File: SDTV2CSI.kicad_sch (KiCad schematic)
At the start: 70 parts, among them J1 Conn_Coaxial, J2 Conn_Coaxial, J3 SFW15R-1STE1LF, J4 5-2301994-9, U1 ADV7280AWBCPZ-M, U2 TLV75718PDBV, U3 XR22800IL32TR-F, U4 MP8007GV-Z, Y1 28.63636MHz

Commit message: update and considering losing poe for waveshare OTS
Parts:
- removed J4: 5-2301994-9, Connector_RJ:RJ45_Bel_SI-60062-F, symbol Connector:RJ45_Bel_SI-60062-F
- added C28, C29: 0.01μF, Capacitor_SMD:C_0402_1005Metric, symbol Device:C_Small
- added D4: BR, Diode_SMD:Diode_Bridge_Diotec_SO-DIL-Slim, symbol Diode_Bridge:DF01S1
- added D5: SBR8U60P5-13, symbol Device:D_Small
- added FB1, FB2: 30m, Inductor_SMD:L_0603_1608Metric, symbol Device:FerriteBead_Small
- added L1: L_Small, symbol Device:L_Small
- added P1: Pi Zero, AU:PIZERO, symbol AU:Pi Zero
- added P2: TMJ19911ADNL, AU:7498210220A, symbol AU:TMJ19911ADNL
- added TR1: CX9628, AU:SMT_29-ALD_COC, symbol AU:CX9628
- J3: footprint AU:528061510 -> AU:CON15_1X15_DRB_SFW_GLE
- R19: value 8.06k -> 7.5k; Alt PN (none) -> CR0402-FX-7501GLF; MPN RC0402FR-078K06L -> WR04X7501FTL; Manufacturer YAGEO -> Walsin Technology Corporation
- R22: value 41.2 -> 576; MPN RC0402FR-0741R2L -> RC0402FR-07576RL
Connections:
- net ER+: now also P2.4 (RD+)
- net ER-: now also P2.6 (RD-)
- net ET+: now also P2.1 (TD+)
- net ET-: now also P2.3 (TD-)
- net at U4.1 (AUX): now also R18.2, R19.1
- net sw: now reaches U4.12 (SW)
- net sw: now also U4.13 (SW__1), TR1.3
- net GNDD: now reaches U4.16 (GND)
- net GNDD: now also U4.17 (GND__1), U4.29 (GND__2), TR1.5
- net VSS: now reaches U4.23 (VSS)
- net VSS: now also U4.24 (VSS__1)
- net at U4.26 (CLASS): now also R22.2
- net VDD: now reaches U4.4 (VDD)
- net VDD: now also R8.1, C29.1, FB1.2, L1.2
- net Vss: now reaches R22.1
- net Vss: now also C29.2, FB2.1
- net SCL renamed CSCL
- net SDA renamed CSDA
- new net: D5.2 (A), TR1.10, TR1.9
- new net: L1.1, TR1.1
- new net CT1: D4.4, P2.2 (CT)
- new net CT2: D4.3, P2.5 (CT)
- new net GNDA: TR1.6, TR1.7
- new net PoEGND: C28.1, D4.2 (-), FB2.2
- new net PoEVDD: C28.2, D4.1 (+), FB1.1
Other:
- moved on the sheet: C1, C10, C11, C12, C13, C14, C15, C16, C17, C18, C19, C2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

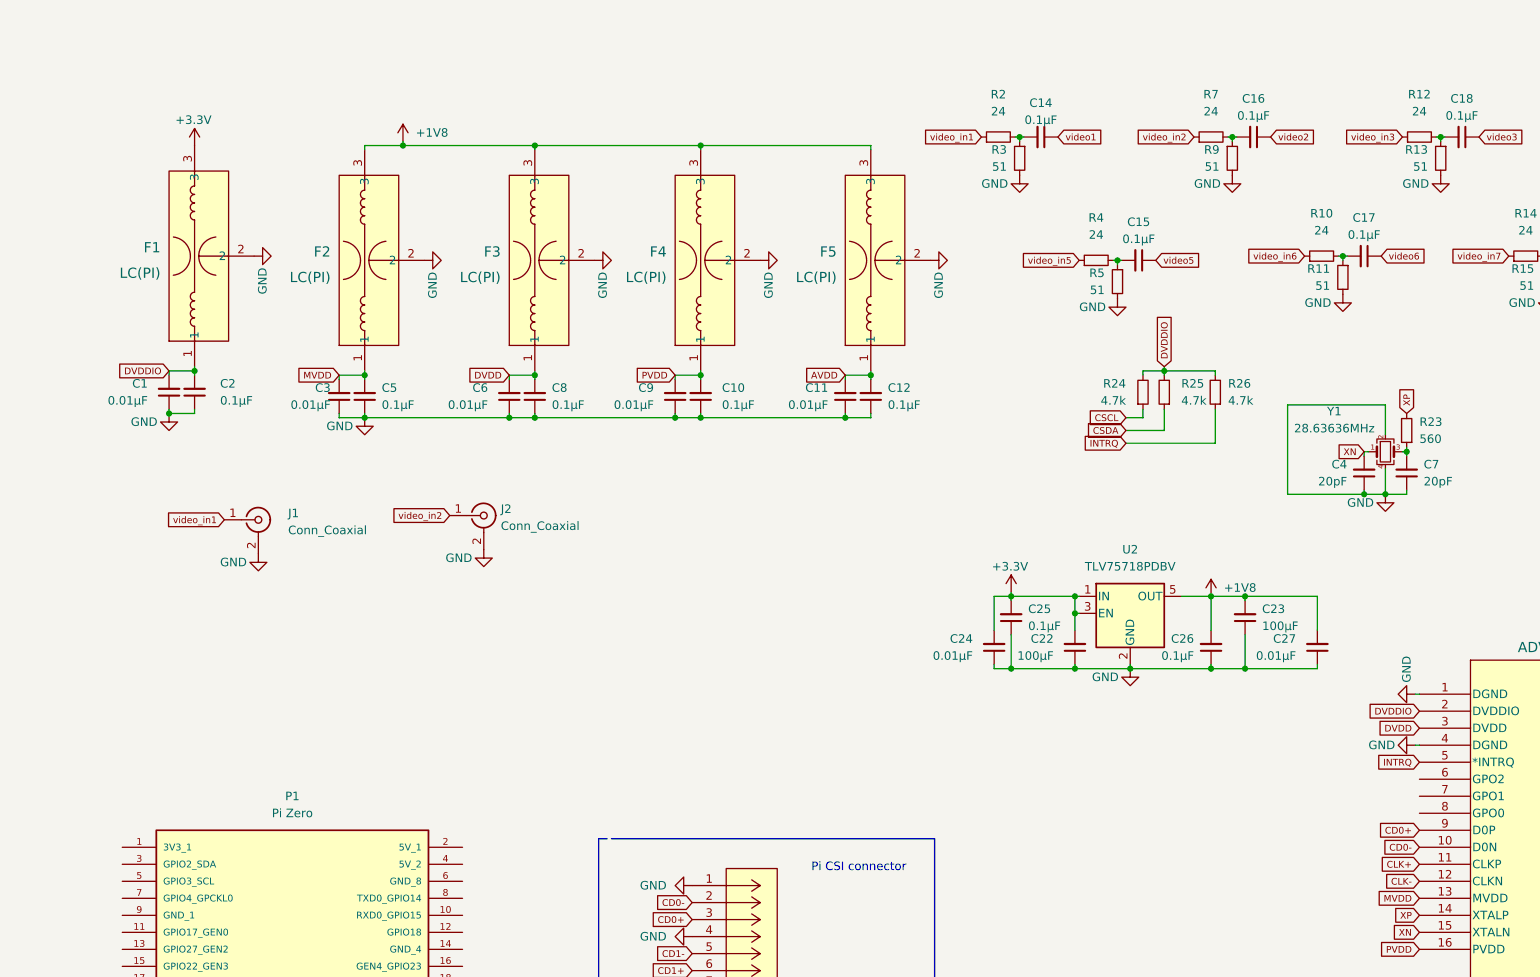
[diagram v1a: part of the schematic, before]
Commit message: working on converting back to 0201
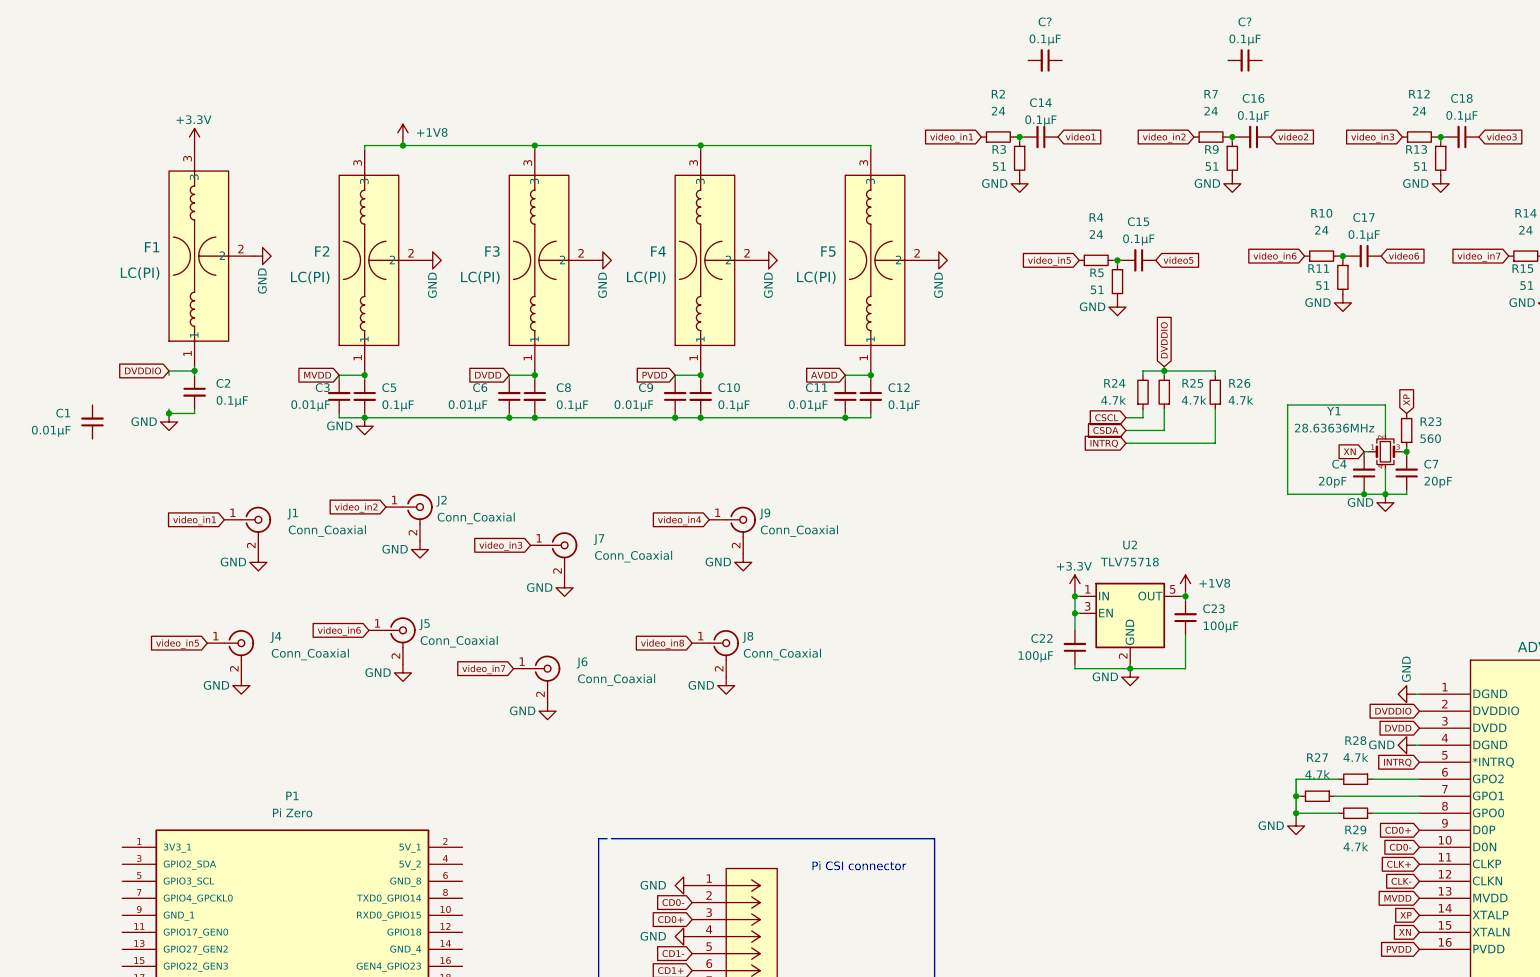
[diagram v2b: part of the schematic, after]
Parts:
- removed C24, C27: 0.01μF, Capacitor_SMD:C_0402_1005Metric, symbol Device:C_Small
- removed C25, C26: 0.1μF, Capacitor_SMD:C_0402_1005Metric, symbol Device:C_Small
- added C? (x2): 0.1μF, AU:R_0201_0603Metric, symbol Device:C_Small
- added J4, J5, J6, J7, J8, J9: Conn_Coaxial, Connector_Coaxial:SMA_Amphenol_901-144_Vertical, symbol Connector:Conn_Coaxial
- added R27, R28, R29: 4.7k, Resistor_SMD:R_0402_1005Metric, symbol Device:R_Small
- C10, C12, C2, C5, C8: footprint Capacitor_SMD:C_0402_1005Metric -> AU:R_0201_0603Metric; JLCPCB PN C60474 -> (none); MPN CC0402KRX7R7BB104 -> GRM033Z71C104KE14D; Manufacturer YAGEO -> Murata Electronics
- U2: value TLV75718PDBV -> TLV75718
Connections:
- net AVDD: now also C12.1; no longer C12.2
- net DVDD: now also C8.1; no longer C8.2
- net DVDDIO: now also C2.1; no longer C1.2, C2.2
- net GND: now also C10.2, C12.2, C2.2, C5.2, C8.2, J4.2 (Ext), J5.2 (Ext), J6.2 (Ext), J7.2 (Ext), J8.2 (Ext), J9.2 (Ext), R27.2, R28.2, R29.2; no longer C1.1, C10.1, C12.1, C2.1, C5.1, C8.1
- net MVDD: now also C5.1; no longer C5.2
- net PVDD: now also C10.1; no longer C10.2
- net video_in3: now also J7.1 (In)
- net video_in4: now also J9.1 (In)
- net video_in5: now also J4.1 (In)
- net video_in6: now also J5.1 (In)
- net video_in7: now also J6.1 (In)
- net video_in8: now also J8.1 (In)
- net at U1.6 (GPO2): now also R28.1
- net at U1.7 (GPO1): now also R27.1
- net at U1.8 (GPO0): now also R29.1
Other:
- moved on the sheet: C1, C23, J2

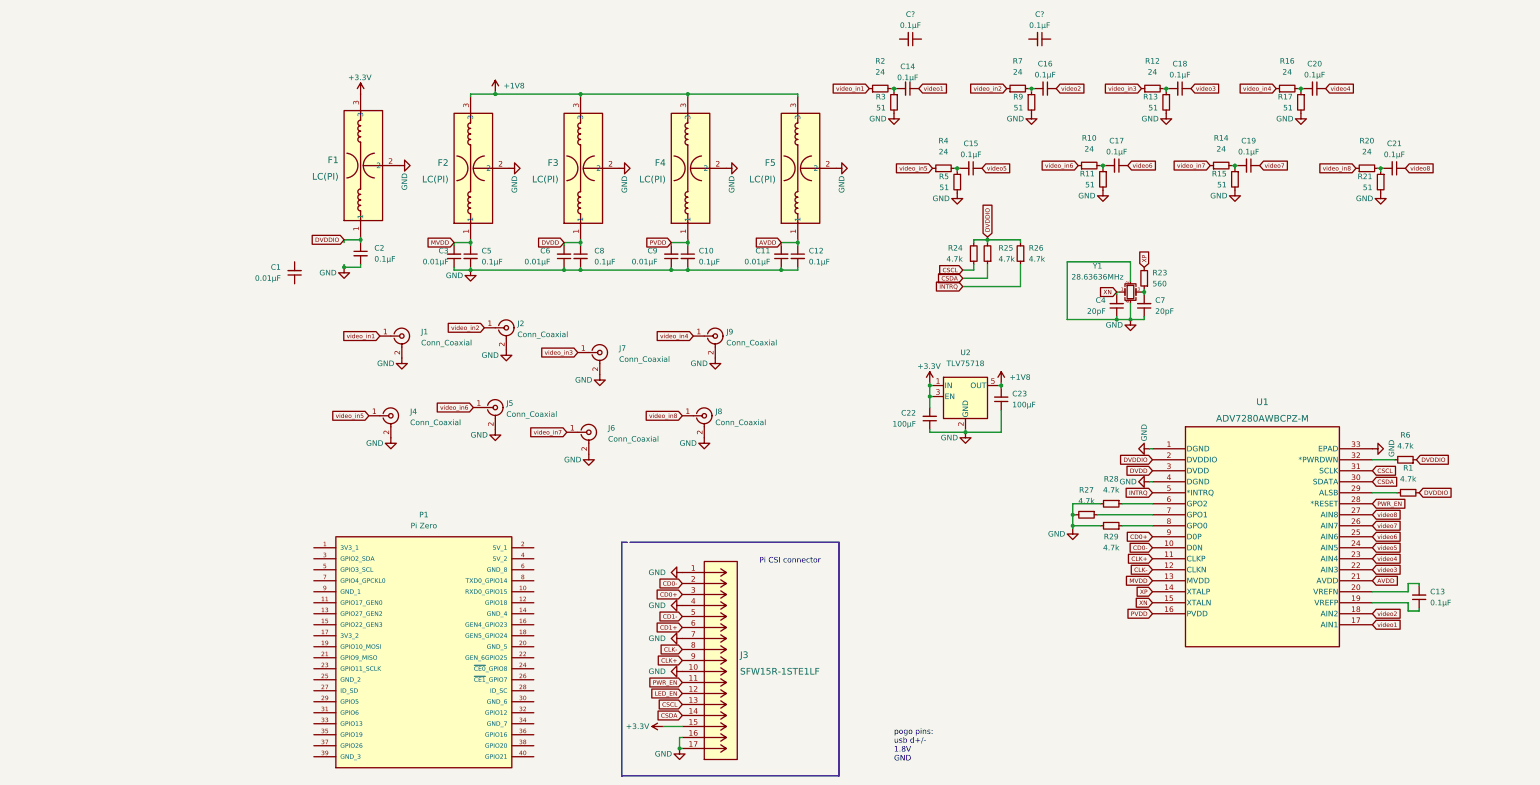
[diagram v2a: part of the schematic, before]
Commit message: will remove PoE components commit for posterity
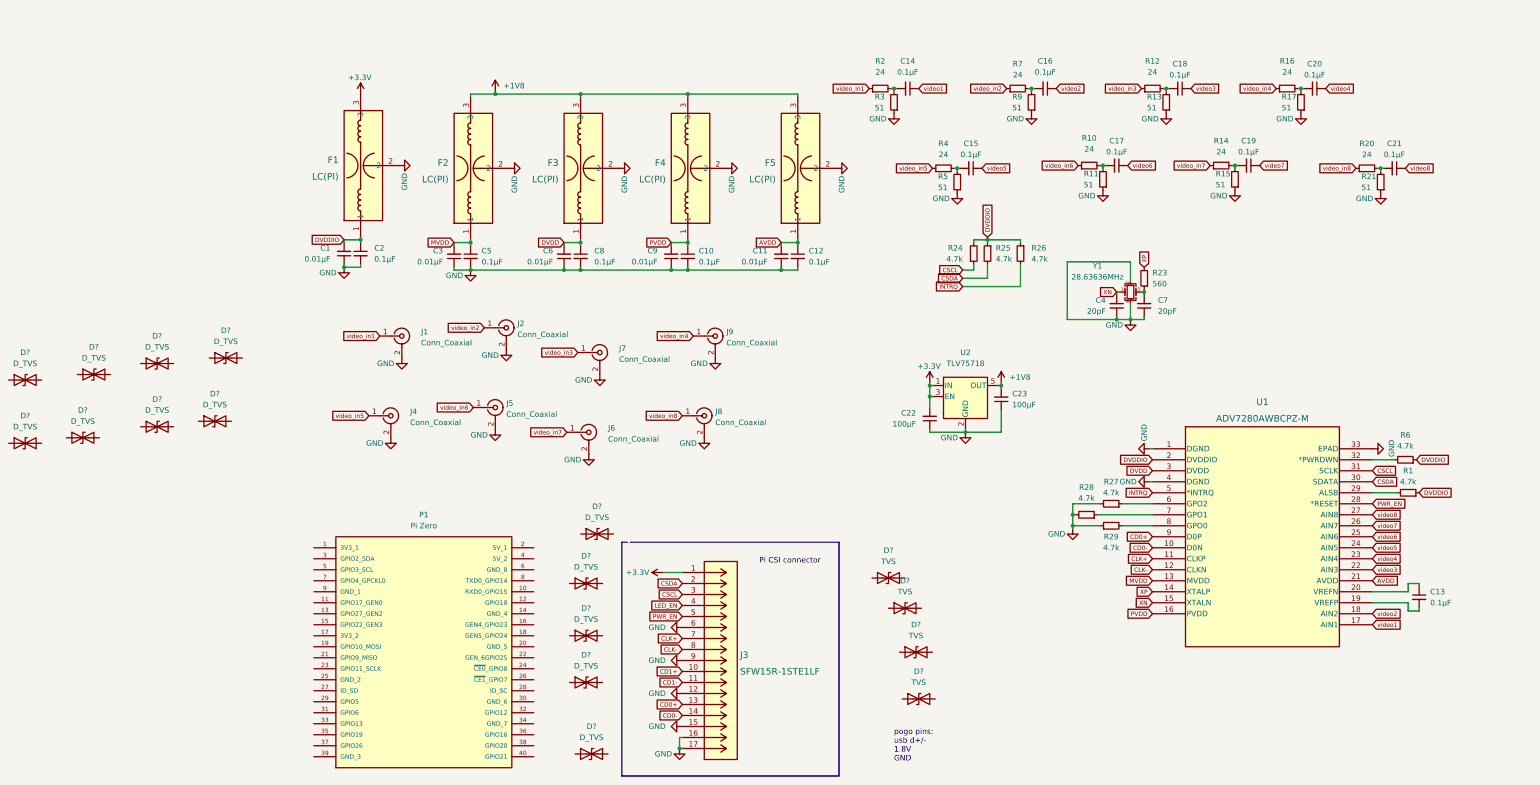
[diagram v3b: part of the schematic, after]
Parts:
- removed C14, C16: 0.1μF, Capacitor_SMD:C_0402_1005Metric, symbol Device:C_Small
- added D? (x13): D_TVS, AU:R_0201_0603Metric, symbol Device:D_TVS
- added D? (x4): TVS, AU:R_0201_0603Metric, symbol Device:D_TVS
- C1, C11, C3, C6, C9: footprint Capacitor_SMD:C_0402_1005Metric -> AU:R_0201_0603Metric; JLCPCB PN C15195 -> (none); MPN CL05B103KB5NNNC -> GRM033R71E103KE14D; Manufacturer Samsung Electro-Mechanics -> Murata Electronics; Voltage 50V -> 25V
- C13: footprint Capacitor_SMD:C_0402_1005Metric -> AU:R_0201_0603Metric; JLCPCB PN C60474 -> (none); MPN CC0402KRX7R7BB104 -> GRM033Z71C104KE14D; Manufacturer YAGEO -> Murata Electronics
- C4, C7: footprint Capacitor_SMD:C_0402_1005Metric -> AU:R_0201_0603Metric; JLCPCB PN C437436 -> (none); MPN GRT1555C1H200FA02D -> GRM0335C1H200GA01D; Tolerance 1% -> (none)
- R1, R24, R25, R26, R27, R28, R29, R6: footprint Resistor_SMD:R_0402_1005Metric -> Resistor_SMD:R_0201_0603Metric; JLCPCB PN C105870 -> (none); MPN RC0402JR-074K7L -> CR0201-JW-472GLF; Manufacturer YAGEO -> Bourns Inc.; Power 1/16W -> 1/20W; Stock on hand (none) -> 10k
- R2, R7: footprint Resistor_SMD:R_0402_1005Metric -> Resistor_SMD:R_0201_0603Metric; JLCPCB PN C274890 -> (none); MPN RT0402FRE0724RL -> ERJ-1GNF24R0C; Manufacturer YAGEO -> Panasonic Electronic Components; Power 1/16W -> 1/20W
- R23: footprint Resistor_SMD:R_0402_1005Metric -> AU:R_0201_0603Metric; Alt PN (none) -> CRCW0201560RFKED; JLCPCB PN C163460 -> (none); MPN CR0402-FX-5600GLF -> ERA-1AEB561C; Manufacturer Bourns Inc. -> Panasonic Electronic Components; Tolerance (none) -> 1%
- R3, R9: footprint Resistor_SMD:R_0402_1005Metric -> Resistor_SMD:R_0201_0603Metric; JLCPCB PN C227127 -> (none); MPN RT0402FRE0751RL -> RMCF0201FT51R0; Manufacturer YAGEO -> Stackpole Electronics Inc; Power 1/16W -> 1/20W
- gave numbers to parts that had none: 2
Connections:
- net +3V3: now also J3.1; no longer J3.15
- net CD0+: now also J3.13; no longer J3.3
- net CD0-: now also J3.14; no longer J3.2
- net CD1+: now also J3.10; no longer J3.6
- net CD1-: now also J3.11; no longer J3.5
- net CLK+: now also J3.7; no longer J3.9
- net CSCL: now also J3.3; no longer J3.13
- net CSDA: now also J3.2, R25.2; no longer J3.14, R25.1
- net DVDDIO: now also C1.2, R1.1, R25.1, R26.1; no longer R1.2, R25.2, R26.2
- net GND: now also C1.1, J3.12, J3.15, J3.6, J3.9, R11.1, R13.1, R15.1, R17.1, R21.1, R29.1, R3.1, R5.1, R9.1; no longer J3.1, J3.10, J3.4, J3.7, R11.2, R13.2, R15.2, R17.2, R21.2, R29.2, R3.2, R5.2, R9.2
- net INTRQ: now also R26.2; no longer R26.1
- net LED_EN: now also J3.4; no longer J3.12
- net PWR_EN: now also J3.5; no longer J3.11
- net video1: now also C14.1
- net video2: now also C16.1
- net at C20.2, R16.2: now also R17.2; no longer R17.1
- net at U1.19 (VREFP): now also C13.2; no longer C13.1
- net at U1.20 (VREFN): now also C13.1; no longer C13.2
- net at R2.2: now also C14.2, R3.2; no longer R3.1
- net at C21.2, R20.2: now also R21.2; no longer R21.1
- net at C18.2, R12.2: now also R13.2; no longer R13.1
- net at U1.29 (ALSB): now also R1.2; no longer R1.1
- net at U1.6 (GPO2): now also R27.1; no longer R28.1
- net at U1.7 (GPO1): now also R28.1; no longer R27.1
- net at U1.8 (GPO0): now also R29.2; no longer R29.1
- net at C15.2, R4.2: now also R5.2; no longer R5.1
- net at R7.2: now also C16.2, R9.2; no longer R9.1
- net at C19.2, R14.2: now also R15.2; no longer R15.1
- net at C17.2, R10.2: now also R11.2; no longer R11.1
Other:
- moved on the sheet: C1, C14, C16
